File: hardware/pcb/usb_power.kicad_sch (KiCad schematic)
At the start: 1 part, among them J4 USB_C_Receptacle_USB2.0

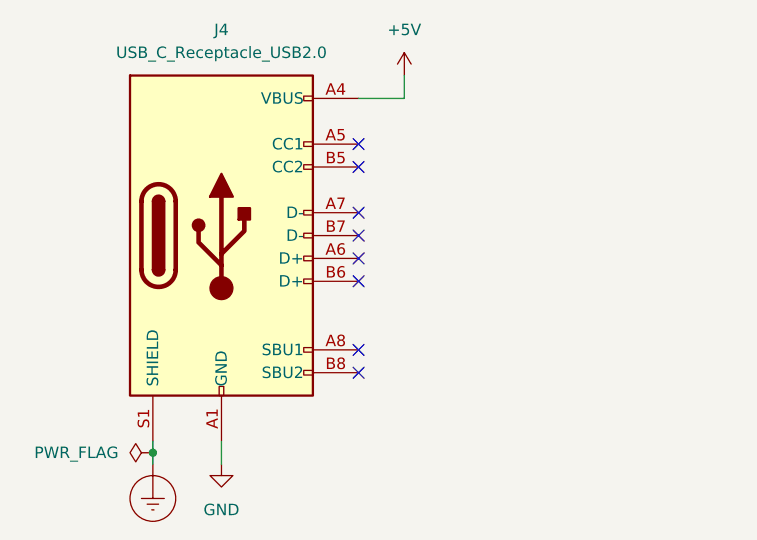
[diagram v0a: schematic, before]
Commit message: Restructuring folder structure
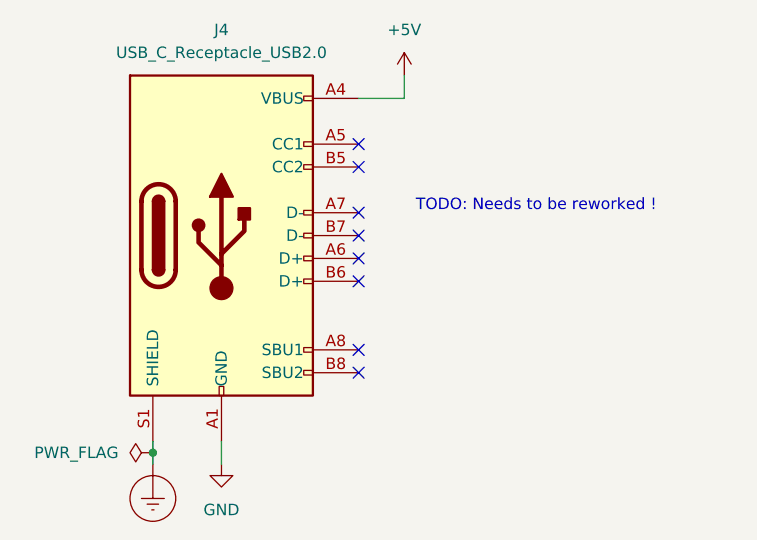
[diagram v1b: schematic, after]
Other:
- note added: "TODO: Needs to be reworked !"
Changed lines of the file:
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@@
     (stroke (width 0) (type default))
+  )
+  (text "TODO: Needs to be reworked !" (at 60.96 40.64 0)
+    (effects (font (size 1.27 1.27)) (justify left bottom))
   )
   (symbol (lib_id "power:Earth_Protective") (at 31.75 68.58 0) (unit 1)

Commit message: Verify workflow after moving files
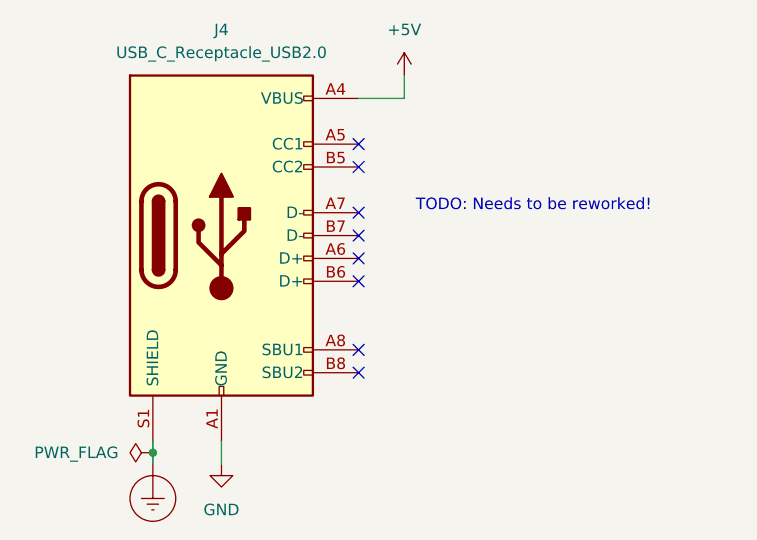
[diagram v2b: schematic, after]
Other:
- note added: "TODO: Needs to be reworked!"
- note removed: "TODO: Needs to be reworked !"
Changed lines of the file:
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@@
     (stroke (width 0) (type default))
   )
-  (text "TODO: Needs to be reworked !" (at 60.96 40.64 0)
+  (text "TODO: Needs to be reworked!" (at 60.96 40.64 0)
     (effects (font (size 1.27 1.27)) (justify left bottom))
   )

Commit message: Testing rerunning kibot
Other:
- note added: "TODO: Needs to be reworked!!!"
- note removed: "TODO: Needs to be reworked!"
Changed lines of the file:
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@@
     (stroke (width 0) (type default))
   )
-  (text "TODO: Needs to be reworked!" (at 60.96 40.64 0)
+  (text "TODO: Needs to be reworked!!!" (at 60.96 40.64 0)
     (effects (font (size 1.27 1.27)) (justify left bottom))
   )

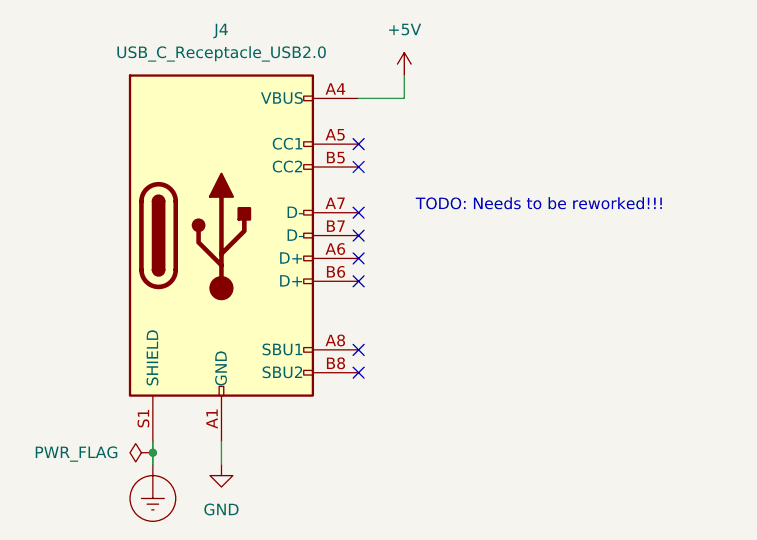
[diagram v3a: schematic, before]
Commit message: Fixing USB-C power connector -> release hardware version v0.3
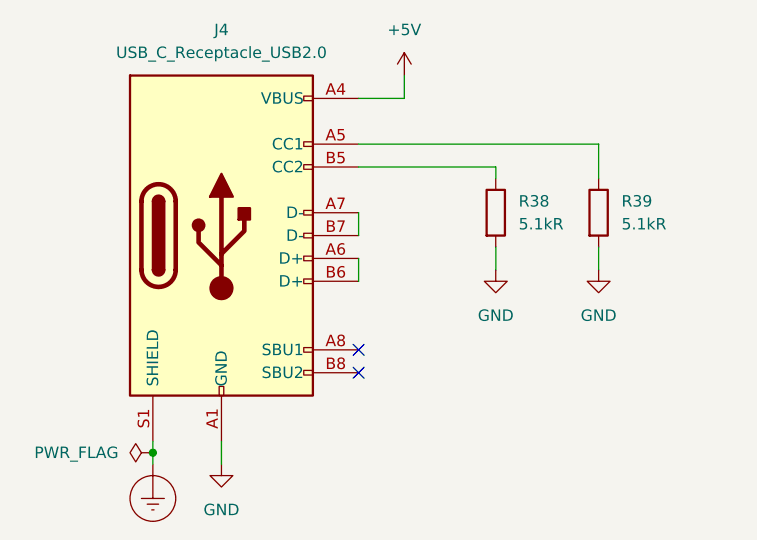
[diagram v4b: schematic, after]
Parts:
- added R38, R39: 5.1kR, Resistor_SMD:R_0805_2012Metric_Pad1.20x1.40mm_HandSolder, symbol Device:R
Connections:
- net GND: now also R38.2, R39.2
- net at J4.A5 (CC1): now also R39.1
- net at J4.A6 (D+): now also J4.B6 (D+)
- net at J4.A7 (D-): now also J4.B7 (D-)
- net at J4.B5 (CC2): now also R38.1
- no-connect marks 8 -> 2
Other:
- note removed: "TODO: Needs to be reworked!!!"
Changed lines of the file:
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@@
   (junction (at 31.75 67.31) (diameter 0) (color 0 0 0 0)
   )
-  (no_connect (at 54.61 45.72))
   (no_connect (at 54.61 58.42))
   (no_connect (at 54.61 55.88))
-  (no_connect (at 54.61 33.02))
-  (no_connect (at 54.61 35.56))
-  (no_connect (at 54.61 43.18))
-  (no_connect (at 54.61 40.64))
-  (no_connect (at 54.61 48.26))
+  (wire (pts (xy 54.61 40.64) (xy 54.61 43.18))
+    (stroke (width 0) (type default))
+  )
+  (wire (pts (xy 81.28 33.02) (xy 54.61 33.02))
+    (stroke (width 0) (type default))
+  )
   (wire (pts (xy 59.69 27.94) (xy 59.69 25.4))
     (stroke (width 0) (type default))
@@
     (stroke (width 0) (type default))
   )
+  (wire (pts (xy 81.28 36.83) (xy 81.28 33.02))
+    (stroke (width 0) (type default))
+  )
+  (wire (pts (xy 54.61 45.72) (xy 54.61 48.26))
+    (stroke (width 0) (type default))
+  )
+  (wire (pts (xy 69.85 36.83) (xy 69.85 35.56))
+    (stroke (width 0) (type default))
+  )
   (wire (pts (xy 31.75 68.58) (xy 31.75 67.31))
     (stroke (width 0) (type default))
@@
     (stroke (width 0) (type default))
   )
+  (wire (pts (xy 54.61 35.56) (xy 69.85 35.56))
+    (stroke (width 0) (type default))
+  )
+  (wire (pts (xy 81.28 46.99) (xy 81.28 44.45))
+    (stroke (width 0) (type default))
+  )
   (wire (pts (xy 31.75 67.31) (xy 31.75 66.04))
     (stroke (width 0) (type default))
   )
-  (text "TODO: Needs to be reworked!!!" (at 60.96 40.64 0)
-    (effects (font (size 1.27 1.27)) (justify left bottom))
+  (wire (pts (xy 69.85 46.99) (xy 69.85 44.45))
+    (stroke (width 0) (type default))
+  )
+  (symbol (lib_id "Device:R") (at 81.28 40.64 0) (unit 1)
+    (in_bom yes) (on_board yes) (dnp no)
+    (property "Reference" "R39" (at 83.82 39.37 0)
+      (effects (font (size 1.27 1.27)) (justify left))
+    )
+    (property "Value" "5.1kR" (at 83.82 41.91 0)
+      (effects (font (size 1.27 1.27)) (justify left))
+    )
+    (property "Footprint" "Resistor_SMD:R_0805_2012Metric_Pad1.20x1.40mm_HandSolder" (at 79.502 40.64 90)
+      (effects (font (size 1.27 1.27)) hide)
+    )
+    (property "Datasheet" "~" (at 81.28 40.64 0)
+      (effects (font (size 1.27 1.27)) hide)
+    )
+    (property "JLCPCB Part #" "C27834" (at 81.28 40.64 90)
+      (effects (font (size 1.27 1.27)) hide)
+    )
+    (pin "2")
+    (pin "1")
+    (instances
+      (project "CybICS"
+        (path "/8fcde287-628f-41a4-bd3a-47641b4dabbc/13fd811d-e525-40d8-9276-ff98ff8345b7"
+          (reference "R39") (unit 1)
+        )
+      )
+    )
   )
   (symbol (lib_id "power:Earth_Protective") (at 31.75 68.58 0) (unit 1)
@@
     )
   )
+  (symbol (lib_id "Device:R") (at 69.85 40.64 0) (unit 1)
+    (in_bom yes) (on_board yes) (dnp no)
+    (property "Reference" "R38" (at 72.39 39.37 0)
+      (effects (font (size 1.27 1.27)) (justify left))
+    )
+    (property "Value" "5.1kR" (at 72.39 41.91 0)
+      (effects (font (size 1.27 1.27)) (justify left))
+    )
+    (property "Footprint" "Resistor_SMD:R_0805_2012Metric_Pad1.20x1.40mm_HandSolder" (at 68.072 40.64 90)
+      (effects (font (size 1.27 1.27)) hide)
+    )
+    (property "Datasheet" "~" (at 69.85 40.64 0)
+      (effects (font (size 1.27 1.27)) hide)
+    )
+    (property "JLCPCB Part #" "C27834" (at 69.85 40.64 90)
+      (effects (font (size 1.27 1.27)) hide)
+    )
+    (pin "2")
+    (pin "1")
+    (instances
+      (project "CybICS"
+        (path "/8fcde287-628f-41a4-bd3a-47641b4dabbc/13fd811d-e525-40d8-9276-ff98ff8345b7"
+          (reference "R38") (unit 1)
+        )
+      )
+    )
+  )
   (symbol (lib_id "power:PWR_FLAG") (at 31.75 67.31 90) (unit 1)
     (in_bom yes) (on_board yes) (dnp no) (fields_autoplaced)
@@
         (path "/8fcde287-628f-41a4-bd3a-47641b4dabbc/13fd811d-e525-40d8-9276-ff98ff8345b7"
           (reference "#FLG04") (unit 1)
+        )
+      )
+    )
+  )
+  (symbol (lib_id "power:GND") (at 81.28 46.99 0) (unit 1)
+    (in_bom yes) (on_board yes) (dnp no) (fields_autoplaced)
+    (property "Reference" "#PWR055" (at 81.28 53.34 0)
+      (effects (font (size 1.27 1.27)) hide)
+    )
+    (property "Value" "GND" (at 81.28 52.07 0)
+      (effects (font (size 1.27 1.27)))
+    )
+    (property "Footprint" "" (at 81.28 46.99 0)
+      (effects (font (size 1.27 1.27)) hide)
+    )
+    (property "Datasheet" "" (at 81.28 46.99 0)
+      (effects (font (size 1.27 1.27)) hide)
+    )
+    (pin "1")
+    (instances
+      (project "CybICS"
+        (path "/8fcde287-628f-41a4-bd3a-47641b4dabbc/13fd811d-e525-40d8-9276-ff98ff8345b7"
+          (reference "#PWR055") (unit 1)
         )
       )
@@
         )
       )
+    )
+  )
+  (symbol (lib_id "power:GND") (at 69.85 46.99 0) (unit 1)
+    (in_bom yes) (on_board yes) (dnp no) (fields_autoplaced)
+    (property "Reference" "#PWR054" (at 69.85 53.34 0)
+      (effects (font (size 1.27 1.27)) hide)
+    )
+    (property "Value" "GND" (at 69.85 52.07 0)
+      (effects (font (size 1.27 1.27)))
+    )
+    (property "Footprint" "" (at 69.85 46.99 0)
+      (effects (font (size 1.27 1.27)) hide)
+    )
+    (property "Datasheet" "" (at 69.85 46.99 0)
+      (effects (font (size 1.27 1.27)) hide)
+    )
+    (pin "1")
+    (instances
+      (project "CybICS"
+        (path "/8fcde287-628f-41a4-bd3a-47641b4dabbc/13fd811d-e525-40d8-9276-ff98ff8345b7"
+          (reference "#PWR054") (unit 1)
+        )
+      )
